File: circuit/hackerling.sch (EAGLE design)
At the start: 45 parts, among them IC1 MCP23017SP, IC2 MCP2300X/P, IC3 MIC5219BM5, SW2 SWITCH_B13EH, U1 MMA8452Q, U2 LCD_16X2, U3 ARDUINOR3-BPLACE, U5 PCA9306, U7 POT

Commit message: tested LCD, works added library to test with - library needs cleaning made some minor changes to the board, removed rx, tx connections
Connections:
- net BTN3: no longer U3.D0
- net BTN4: no longer U3.D1
- net GND: now also B1.S1, B3.S1, B4.S, B4.S1
- net IR_OUT1: now also U3.D6; no longer U3.D5
- net IR_OUT2: now also U3.D5; no longer U3.D6
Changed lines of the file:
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@@
 <wire x1="-82.55" y1="1.27" x2="-92.71" y2="1.27" width="0.1524" layer="91"/>
 <junction x="-92.71" y="1.27"/>
+<wire x1="-92.71" y1="1.27" x2="-104.14" y2="1.27" width="0.1524" layer="91"/>
+<pinref part="B1" gate="G$1" pin="S1"/>
+<wire x1="-104.14" y1="1.27" x2="-104.14" y2="3.81" width="0.1524" layer="91"/>
+<wire x1="-104.14" y1="3.81" x2="-105.41" y2="3.81" width="0.1524" layer="91"/>
+<wire x1="-82.55" y1="1.27" x2="-80.01" y2="1.27" width="0.1524" layer="91"/>
+<junction x="-82.55" y="1.27"/>
+<pinref part="B4" gate="G$1" pin="S"/>
+<wire x1="-80.01" y1="1.27" x2="-71.12" y2="1.27" width="0.1524" layer="91"/>
+<wire x1="-71.12" y1="1.27" x2="-71.12" y2="3.81" width="0.1524" layer="91"/>
+<wire x1="-71.12" y1="3.81" x2="-69.85" y2="3.81" width="0.1524" layer="91"/>
+<pinref part="B3" gate="G$1" pin="S1"/>
+<wire x1="-80.01" y1="3.81" x2="-80.01" y2="1.27" width="0.1524" layer="91"/>
+<junction x="-80.01" y="1.27"/>
+<pinref part="B4" gate="G$1" pin="S1"/>
+<wire x1="-67.31" y1="3.81" x2="-67.31" y2="1.27" width="0.1524" layer="91"/>
+<wire x1="-67.31" y1="1.27" x2="-71.12" y2="1.27" width="0.1524" layer="91"/>
+<junction x="-71.12" y="1.27"/>
 </segment>
 </net>
@@
 <wire x1="-80.01" y1="15.24" x2="-80.01" y2="13.97" width="0.1524" layer="91"/>
 </segment>
-<segment>
-<wire x1="24.13" y1="55.88" x2="10.16" y2="55.88" width="0.1524" layer="91"/>
-<label x="13.97" y="55.88" size="1.778" layer="95"/>
-<pinref part="U3" gate="G$1" pin="D0"/>
-</segment>
 </net>
 <net name="BTN4" class="0">
@@
 <label x="-67.31" y="21.59" size="1.778" layer="95" rot="MR180"/>
 <pinref part="B4" gate="G$1" pin="P1"/>
-</segment>
-<segment>
-<wire x1="24.13" y1="53.34" x2="12.7" y2="53.34" width="0.1524" layer="91"/>
-<label x="13.97" y="53.34" size="1.778" layer="95"/>
-<pinref part="U3" gate="G$1" pin="D1"/>
 </segment>
 </net>
@@
 <net name="IR_OUT1" class="0">
 <segment>
-<pinref part="U3" gate="G$1" pin="D5"/>
-<wire x1="24.13" y1="43.18" x2="13.97" y2="43.18" width="0.1524" layer="91"/>
-<label x="15.24" y="43.18" size="1.778" layer="95"/>
+<wire x1="19.05" y1="44.45" x2="19.05" y2="43.18" width="0.1524" layer="91"/>
+<wire x1="19.05" y1="43.18" x2="3.81" y2="43.18" width="0.1524" layer="91"/>
+<label x="3.81" y="43.18" size="1.778" layer="95"/>
+<wire x1="19.05" y1="44.45" x2="21.59" y2="44.45" width="0.1524" layer="91"/>
+<wire x1="21.59" y1="44.45" x2="21.59" y2="40.64" width="0.1524" layer="91"/>
+<pinref part="U3" gate="G$1" pin="D6"/>
+<wire x1="21.59" y1="40.64" x2="24.13" y2="40.64" width="0.1524" layer="91"/>
 </segment>
 <segment>
@@
 <net name="IR_OUT2" class="0">
 <segment>
-<pinref part="U3" gate="G$1" pin="D6"/>
-<wire x1="24.13" y1="40.64" x2="13.97" y2="40.64" width="0.1524" layer="91"/>
-<label x="15.24" y="40.64" size="1.778" layer="95"/>
-</segment>
-<segment>
+<wire x1="24.13" y1="41.91" x2="19.05" y2="41.91" width="0.1524" layer="91"/>
+<wire x1="19.05" y1="41.91" x2="19.05" y2="40.64" width="0.1524" layer="91"/>
+<wire x1="19.05" y1="40.64" x2="3.81" y2="40.64" width="0.1524" layer="91"/>
+<label x="3.81" y="40.64" size="1.778" layer="95"/>
+<pinref part="U3" gate="G$1" pin="D5"/>
+<wire x1="24.13" y1="41.91" x2="24.13" y2="43.18" width="0.1524" layer="91"/>
+</segment>
+<segment>

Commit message: tested MCP23008, works changed buttons to connect to MCP23017 rerouted stuff
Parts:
- added RN1: (no value), resistor-sil:E5R
- R7: device rcl:R-US_R0603 -> rcl:R-US_R0805
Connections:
- removed net N$5: IC1.GPB3, U2.DB3
- removed net N$6: IC1.GPB2, U2.DB2
- removed net N$7: IC1.GPB1, U2.DB1
- removed net N$8: IC1.GPB0, U2.DB0
- removed net N$9: IC1.GPA5, U2.E
- new net LCD_EN: IC1.GPB3, U2.E, U3.D13
- net BTN1: now also IC1.GPB0; no longer U3.D4
- net BTN2: now also IC1.GPA6; no longer U3.D7
- net BTN3: now also IC1.GPA5
- net BTN4: now also IC1.GPA7
- net GND: now also B2.S
- net N$10: now also IC1.GPB1; no longer IC1.GPA7
- net N$11: now also IC1.GPB2; no longer IC1.GPA6
- net SWITCH: now also U3.D4; no longer U3.D13
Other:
- note added: "Btn1"
- note added: "Btn2"
- note added: "Btn3"
- note added: "Btn4"
- note added: "TODO: add solder jumper"
- note added: "Two ways to actuate LCD_En"
- note added: "Unconnected"

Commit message: circuit state upon submit of version 1.0
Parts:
- removed RN1: (no value), resistor-sil:E5R
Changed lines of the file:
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@@
 <part name="LED3" library="SparkFun" deviceset="LED" device="5MM"/>
 <part name="GND19" library="supply1" deviceset="GND" device=""/>
-<part name="RN1" library="resistor-sil" deviceset="E5R" device=""/>
 </parts>
 <sheets>
@@
 <instance part="LED3" gate="G$1" x="57.15" y="137.16"/>
 <instance part="GND19" gate="1" x="-91.44" y="-3.81" rot="MR0"/>
-<instance part="RN1" gate="A" x="177.8" y="148.59"/>
-<instance part="RN1" gate="B" x="177.8" y="140.97"/>
-<instance part="RN1" gate="C" x="177.8" y="133.35"/>
-<instance part="RN1" gate="D" x="177.8" y="125.73"/>
-<instance part="RN1" gate="E" x="177.8" y="118.11"/>
 </instances>
 <busses>

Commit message: resubmitting circuit version 1.1 was held for drill overlap modified board slightly, mostly in soldermask to improve readability the ir reciever shifted, and moved a few vias.
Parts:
- removed H1, H3, H4: MOUNTHOLE'3.2, hackerscouts:MOUNTHOLE'3.2
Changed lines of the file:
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@@
 <part name="GND11" library="supply1" deviceset="GND" device=""/>
 <part name="H2" library="hackerscouts" deviceset="MOUNTHOLE" device="'3.2"/>
-<part name="H1" library="hackerscouts" deviceset="MOUNTHOLE" device="'3.2"/>
-<part name="H3" library="hackerscouts" deviceset="MOUNTHOLE" device="'3.2"/>
 <part name="R3" library="SparkFun" deviceset="RESISTOR" device="0603-RES" value="4k7"/>
 <part name="GND12" library="SparkFun" deviceset="GND" device=""/>
@@
 <part name="P+16" library="supply1" deviceset="VCC" device=""/>
 <part name="GND17" library="supply1" deviceset="GND" device=""/>
-<part name="H4" library="hackerscouts" deviceset="MOUNTHOLE" device="'3.2"/>
 <part name="B1" library="hackerscouts" deviceset="SWITCH_BCF-4000" device=""/>
 <part name="B2" library="hackerscouts" deviceset="SWITCH_BCF-4000" device=""/>
@@
 <instance part="GND11" gate="1" x="73.66" y="-40.64"/>
 <instance part="H2" gate="G$1" x="49.53" y="-50.8"/>
-<instance part="H1" gate="G$1" x="49.53" y="-58.42"/>
-<instance part="H3" gate="G$1" x="49.53" y="-66.04"/>
 <instance part="R3" gate="G$1" x="439.42" y="43.18" rot="R90"/>
 <instance part="GND12" gate="1" x="396.24" y="60.96"/>
@@
 <instance part="P+16" gate="VCC" x="-22.86" y="2.54"/>
 <instance part="GND17" gate="1" x="-50.8" y="-17.78" rot="MR0"/>
-<instance part="H4" gate="G$1" x="49.53" y="-76.2"/>
 <instance part="B1" gate="G$1" x="-113.03" y="6.35" rot="MR180"/>
 <instance part="B2" gate="G$1" x="-100.33" y="6.35" rot="MR180"/>

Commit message: documenting updated values in eagle files filled out BOM writing installation instructions
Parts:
- C5: value (none) -> 10uF
- renumbered U$3 to U4, U$6 to U6, U$8 to U8
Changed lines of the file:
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@@
 <part name="GND9" library="supply1" deviceset="GND" device=""/>
 <part name="P+8" library="supply1" deviceset="VCC" device=""/>
-<part name="U$3" library="hackerscouts" deviceset="ACCELEROMETER" device=""/>
+<part name="U4" library="hackerscouts" deviceset="ACCELEROMETER" device=""/>
 <part name="GND10" library="supply1" deviceset="GND" device=""/>
 <part name="P+10" library="supply1" deviceset="VCC" device=""/>
@@
 <part name="R5" library="SparkFun" deviceset="RESISTOR" device="0603-RES" value="200K"/>
 <part name="P+15" library="SparkFun" deviceset="3.3V" device=""/>
-<part name="U$6" library="hackerscouts" deviceset="ACCELEROMETER" device=""/>
+<part name="U6" library="hackerscouts" deviceset="ACCELEROMETER" device=""/>
 <part name="U7" library="hackerscouts" deviceset="POT" device=""/>
 <part name="P+16" library="supply1" deviceset="VCC" device=""/>
@@
 <part name="SW2" library="hackerscouts" deviceset="SWITCH_B13EH" device=""/>
 <part name="GND18" library="supply1" deviceset="GND" device=""/>
-<part name="U$8" library="hackerscouts" deviceset="SML_POT" device=""/>
+<part name="U8" library="hackerscouts" deviceset="SML_POT" device=""/>
 <part name="P+17" library="supply1" deviceset="VCC" device=""/>
 <part name="C4" library="rcl" deviceset="C-US" device="050-050X075" value="10uF"/>
 <part name="R6" library="resistor" deviceset="R-US_" device="0204/7" value="47"/>
 <part name="R7" library="rcl" deviceset="R-US_" device="R0805"/>
-<part name="C5" library="resistor" deviceset="C-US" device="C0805K"/>
+<part name="C5" library="resistor" deviceset="C-US" device="C0805K" value="10uF"/>
 <part name="JP1" library="SparkFun" deviceset="M02" device="LOCK"/>
 <part name="JP2" library="SparkFun" deviceset="M02" device="LOCK"/>
@@
 <instance part="GND9" gate="1" x="-20.32" y="82.55"/>
 <instance part="P+8" gate="VCC" x="10.16" y="106.68"/>
-<instance part="U$3" gate="G$1" x="-20.32" y="25.4" rot="MR0"/>
+<instance part="U4" gate="G$1" x="-20.32" y="25.4" rot="MR0"/>
 <instance part="GND10" gate="1" x="-35.56" y="22.86" rot="MR0"/>
 <instance part="P+10" gate="VCC" x="-96.52" y="38.1"/>
@@
 <instance part="R5" gate="G$1" x="370.84" y="91.44" rot="R90"/>
 <instance part="P+15" gate="G$1" x="426.72" y="58.42"/>
-<instance part="U$6" gate="G$1" x="-40.64" y="-12.7" rot="MR0"/>
+<instance part="U6" gate="G$1" x="-40.64" y="-12.7" rot="MR0"/>
 <instance part="U7" gate="G$1" x="50.8" y="86.36"/>
 <instance part="P+16" gate="VCC" x="-22.86" y="2.54"/>
@@
 <instance part="SW2" gate="G$1" x="-63.5" y="45.72"/>
 <instance part="GND18" gate="1" x="-40.64" y="41.91" rot="MR0"/>
-<instance part="U$8" gate="G$1" x="180.34" y="68.58" rot="MR180"/>
+<instance part="U8" gate="G$1" x="180.34" y="68.58" rot="MR180"/>
 <instance part="P+17" gate="VCC" x="185.42" y="25.4"/>
 <instance part="C4" gate="G$1" x="-16.51" y="101.6"/>
@@
 </segment>
 <segment>
-<pinref part="U$3" gate="G$1" pin="GND"/>
+<pinref part="U4" gate="G$1" pin="GND"/>
 <wire x1="-30.48" y1="27.94" x2="-43.18" y2="27.94" width="0.1524" layer="91"/>
 <wire x1="-43.18" y1="27.94" x2="-43.18" y2="26.67" width="0.1524" layer="91"/>
@@
 </segment>
 <segment>
-<pinref part="U$6" gate="G$1" pin="GND"/>
+<pinref part="U6" gate="G$1" pin="GND"/>
 <pinref part="GND17" gate="1" pin="GND"/>
 <wire x1="-50.8" y1="-15.24" x2="-50.8" y2="-10.16" width="0.1524" layer="91"/>
@@
 <wire x1="193.04" y1="58.42" x2="180.34" y2="58.42" width="0.1524" layer="91"/>
 <wire x1="180.34" y1="58.42" x2="180.34" y2="57.15" width="0.1524" layer="91"/>
-<pinref part="U$8" gate="G$1" pin="E"/>
+<pinref part="U8" gate="G$1" pin="E"/>
 <wire x1="180.34" y1="60.96" x2="180.34" y2="58.42" width="0.1524" layer="91"/>
 <junction x="180.34" y="58.42"/>
@@
 <pinref part="P+9" gate="VCC" pin="VCC"/>
 <wire x1="-2.54" y1="38.1" x2="-5.08" y2="38.1" width="0.1524" layer="91"/>
-<pinref part="U$3" gate="G$1" pin="+5V"/>
+<pinref part="U4" gate="G$1" pin="+5V"/>
 <wire x1="-2.54" y1="33.02" x2="-2.54" y2="38.1" width="0.1524" layer="91"/>
 <wire x1="-22.86" y1="-5.08" x2="-22.86" y2="0" width="0.1524" layer="91"/>
 <pinref part="P+16" gate="VCC" pin="VCC"/>
-<pinref part="U$6" gate="G$1" pin="+5V"/>
+<pinref part="U6" gate="G$1" pin="+5V"/>
 </segment>
 <segment>
@@
 <wire x1="193.04" y1="55.88" x2="190.5" y2="55.88" width="0.1524" layer="91"/>
 <wire x1="190.5" y1="55.88" x2="190.5" y2="78.74" width="0.1524" layer="91"/>
-<pinref part="U$8" gate="G$1" pin="A"/>
+<pinref part="U8" gate="G$1" pin="A"/>
 <wire x1="190.5" y1="78.74" x2="190.5" y2="83.82" width="0.1524" layer="91"/>
 <wire x1="190.5" y1="78.74" x2="180.34" y2="78.74" width="0.1524" layer="91"/>
@@
 </segment>
 <segment>
-<pinref part="U$3" gate="G$1" pin="SCL"/>
+<pinref part="U4" gate="G$1" pin="SCL"/>
 <wire x1="-30.48" y1="33.02" x2="-41.91" y2="33.02" width="0.1524" layer="91"/>
 <label x="-39.37" y="33.02" size="1.778" layer="95"/>
@@
 </segment>
 <segment>
-<pinref part="U$3" gate="G$1" pin="SDA"/>
+<pinref part="U4" gate="G$1" pin="SDA"/>
 <wire x1="-30.48" y1="30.48" x2="-41.91" y2="30.48" width="0.1524" layer="91"/>
 <label x="-39.37" y="30.48" size="1.778" layer="95"/>
@@
 <net name="A_INT2" class="0">
 <segment>
-<pinref part="U$3" gate="G$1" pin="INT2"/>
+<pinref part="U4" gate="G$1" pin="INT2"/>
 <wire x1="3.81" y1="30.48" x2="-2.54" y2="30.48" width="0.1524" layer="91"/>
 <label x="-1.27" y="30.48" size="1.778" layer="95"/>
 <wire x1="-16.51" y1="-7.62" x2="-22.86" y2="-7.62" width="0.1524" layer="91"/>
-<pinref part="U$6" gate="G$1" pin="INT2"/>
+<pinref part="U6" gate="G$1" pin="INT2"/>
 <label x="-20.32" y="-7.62" size="1.778" layer="95"/>
 </segment>
@@
 <net name="A_INT1" class="0">
 <segment>
-<pinref part="U$3" gate="G$1" pin="INT1"/>
+<pinref part="U4" gate="G$1" pin="INT1"/>
 <wire x1="3.81" y1="27.94" x2="-2.54" y2="27.94" width="0.1524" layer="91"/>
 <label x="-1.27" y="27.94" size="1.778" layer="95"/>
 <wire x1="-16.51" y1="-10.16" x2="-22.86" y2="-10.16" width="0.1524" layer="91"/>
-<pinref part="U$6" gate="G$1" pin="INT1"/>
+<pinref part="U6" gate="G$1" pin="INT1"/>
 <label x="-20.32" y="-10.16" size="1.778" layer="95"/>
 </segment>
@@
 </segment>
 <segment>
-<pinref part="U$6" gate="G$1" pin="SCL"/>
+<pinref part="U6" gate="G$1" pin="SCL"/>
 <wire x1="-50.8" y1="-5.08" x2="-66.04" y2="-5.08" width="0.1524" layer="91"/>
 <label x="-60.96" y="-5.08" size="1.778" layer="95"/>
@@
 </segment>
 <segment>
-<pinref part="U$6" gate="G$1" pin="SDA"/>
+<pinref part="U6" gate="G$1" pin="SDA"/>
 <wire x1="-50.8" y1="-7.62" x2="-66.04" y2="-7.62" width="0.1524" layer="91"/>
 <label x="-60.96" y="-7.62" size="1.778" layer="95"/>
@@
 <pinref part="U2" gate="G$1" pin="VO"/>
 <wire x1="187.96" y1="53.34" x2="193.04" y2="53.34" width="0.1524" layer="91"/>
-<pinref part="U$8" gate="G$1" pin="S"/>
-</segment>
-</net>
+<pinref part="U8" gate="G$1" pin="S"/>
+</segment>
+</net>

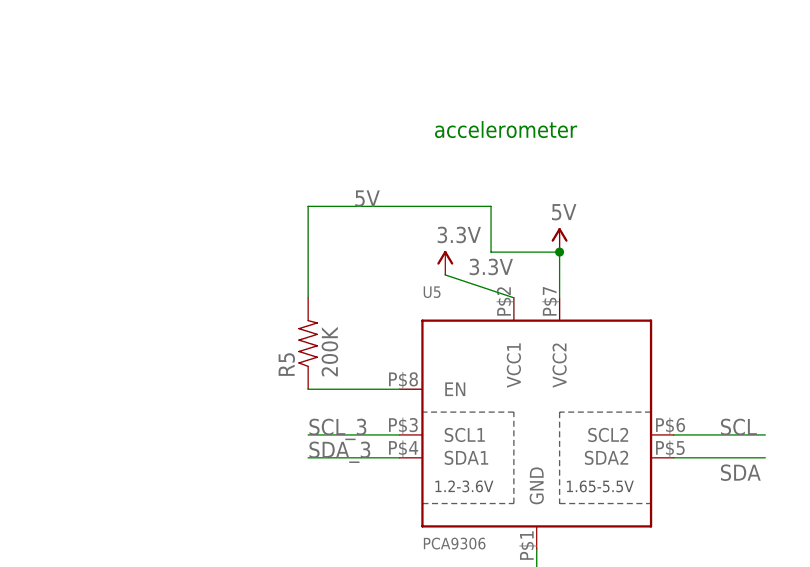
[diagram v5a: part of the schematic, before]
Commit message: power change to accelerometer section
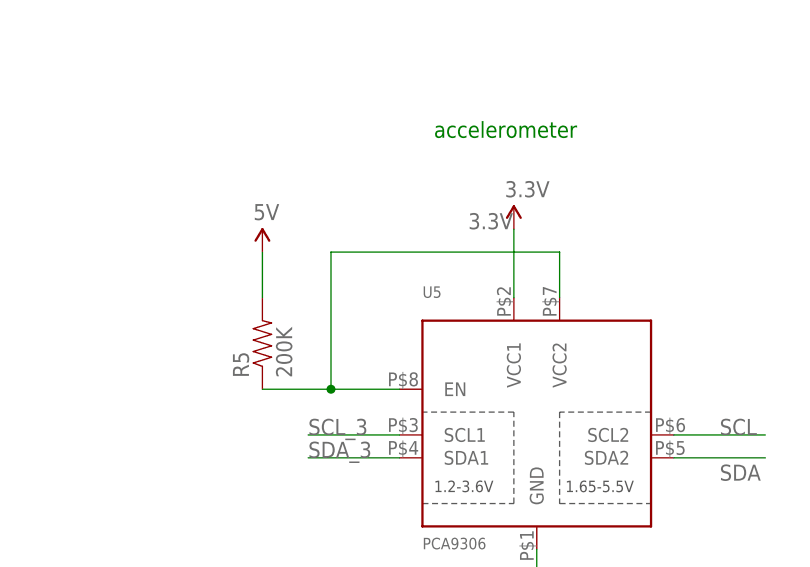
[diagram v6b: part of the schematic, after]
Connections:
- removed net 5V: R5.2, U5.VCC2
- removed net N$27: R5.1, U5.EN
- new net N$5: R5.1, U5.EN, U5.VCC2
- net VCC: now also R5.2
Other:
- moved on the sheet: R5
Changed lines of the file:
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@@
 <?xml version="1.0" encoding="utf-8"?>
 <!DOCTYPE eagle SYSTEM "eagle.dtd">
-<eagle version="6.2">
+<eagle version="6.4">
 <drawing>
 <settings>
@@
 <setting verticaltext="up"/>
 </settings>
-<grid distance="0.05" unitdist="inch" unit="inch" style="lines" multiple="1" display="no" altdistance="0.01" altunitdist="inch" altunit="inch"/>
+<grid distance="0.1" unitdist="inch" unit="inch" style="lines" multiple="1" display="no" altdistance="0.01" altunitdist="inch" altunit="inch"/>
 <layers>
 <layer number="1" name="Top" color="4" fill="1" visible="no" active="no"/>
@@
 <part name="U1" library="hackerscouts" deviceset="MMA8452Q" device=""/>
 <part name="P+14" library="SparkFun" deviceset="3.3V" device=""/>
-<part name="U$4" library="SparkFun" deviceset="5V" device=""/>
 <part name="C2" library="resistor" deviceset="C-US" device="C0603K" value="0.1uF"/>
 <part name="C3" library="resistor" deviceset="C-US" device="C0603K" value="4.7uF"/>
@@
 <part name="LED3" library="SparkFun" deviceset="LED" device="5MM"/>
 <part name="GND19" library="supply1" deviceset="GND" device=""/>
+<part name="VCC" library="SparkFun" deviceset="5V" device=""/>
 </parts>
 <sheets>
@@
 <instance part="GND16" gate="1" x="431.8" y="40.64"/>
 <instance part="U1" gate="G$1" x="401.32" y="35.56"/>
-<instance part="P+14" gate="G$1" x="386.08" y="99.06"/>
-<instance part="U$4" gate="G$1" x="398.78" y="101.6"/>
+<instance part="P+14" gate="G$1" x="393.7" y="104.14"/>
 <instance part="C2" gate="G$1" x="381" y="35.56"/>
 <instance part="C3" gate="G$1" x="429.26" y="50.8"/>
 <instance part="R4" gate="G$1" x="447.04" y="43.18" rot="R90"/>
 <instance part="U5" gate="G$1" x="396.24" y="83.82"/>
-<instance part="R5" gate="G$1" x="370.84" y="91.44" rot="R90"/>
+<instance part="R5" gate="G$1" x="365.76" y="91.44" rot="R90"/>
 <instance part="P+15" gate="G$1" x="426.72" y="58.42"/>
 <instance part="U6" gate="G$1" x="-40.64" y="-12.7" rot="MR0"/>
@@
 <instance part="LED3" gate="G$1" x="57.15" y="137.16"/>
 <instance part="GND19" gate="1" x="-91.44" y="-3.81" rot="MR0"/>
+<instance part="VCC" gate="G$1" x="365.76" y="101.6"/>
 </instances>
 <busses>
@@
 <junction x="10.16" y="104.14"/>
 </segment>
+<segment>
+<pinref part="R5" gate="G$1" pin="2"/>
+<pinref part="VCC" gate="G$1" pin="5V"/>
+<wire x1="365.76" y1="101.6" x2="365.76" y2="96.52" width="0.1524" layer="91"/>
+</segment>
 </net>
 <net name="SCL" class="0">
@@
 <segment>
 <pinref part="P+14" gate="G$1" pin="3.3V"/>
-<wire x1="386.08" y1="99.06" x2="393.7" y2="96.52" width="0.1524" layer="91"/>
+<wire x1="393.7" y1="104.14" x2="393.7" y2="96.52" width="0.1524" layer="91"/>
 <pinref part="U5" gate="G$1" pin="VCC1"/>
-<label x="388.62" y="99.06" size="1.778" layer="95"/>
+<label x="388.62" y="104.14" size="1.778" layer="95"/>
 </segment>
 <segment>
@@
 </segment>
 </net>
-<net name="5V" class="0">
-<segment>
-<pinref part="U5" gate="G$1" pin="VCC2"/>
-<wire x1="398.78" y1="96.52" x2="398.78" y2="101.6" width="0.1524" layer="91"/>
-<pinref part="U$4" gate="G$1" pin="5V"/>
-<junction x="398.78" y="101.6"/>
-<wire x1="391.16" y1="101.6" x2="398.78" y2="101.6" width="0.1524" layer="91"/>
-<wire x1="391.16" y1="106.68" x2="391.16" y2="101.6" width="0.1524" layer="91"/>
-<wire x1="370.84" y1="106.68" x2="391.16" y2="106.68" width="0.1524" layer="91"/>
-<pinref part="R5" gate="G$1" pin="2"/>
-<wire x1="370.84" y1="96.52" x2="370.84" y2="106.68" width="0.1524" layer="91"/>
-<label x="375.92" y="106.68" size="1.778" layer="95"/>
-</segment>
-</net>
 <net name="SCL_3" class="0">
 <segment>
@@
 <pinref part="C2" gate="G$1" pin="1"/>
 <wire x1="383.54" y1="38.1" x2="381" y2="38.1" width="0.1524" layer="91"/>
-</segment>
-</net>
-<net name="N$27" class="0">
-<segment>
-<pinref part="U5" gate="G$1" pin="EN"/>
-<pinref part="R5" gate="G$1" pin="1"/>
-<wire x1="381" y1="86.36" x2="370.84" y2="86.36" width="0.1524" layer="91"/>
 </segment>
 </net>
@@
 </segment>
 </net>
+<net name="N$5" class="0">
+<segment>
+<pinref part="U5" gate="G$1" pin="VCC2"/>
+<wire x1="398.78" y1="96.52" x2="398.78" y2="101.6" width="0.1524" layer="91"/>
+<pinref part="U5" gate="G$1" pin="EN"/>
+<pinref part="R5" gate="G$1" pin="1"/>
+<wire x1="381" y1="86.36" x2="373.38" y2="86.36" width="0.1524" layer="91"/>
+<wire x1="373.38" y1="86.36" x2="365.76" y2="86.36" width="0.1524" layer="91"/>
+<wire x1="398.78" y1="101.6" x2="373.38" y2="101.6" width="0.1524" layer="91"/>
+<wire x1="373.38" y1="101.6" x2="373.38" y2="86.36" width="0.1524" layer="91"/>
+<junction x="373.38" y="86.36"/>
+</segment>
+</net>
